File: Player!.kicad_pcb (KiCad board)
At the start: 2 copper layers, 95.2 x 38.1 mm, 25 parts, among them J1 USB4085-GF-A_REVA4, SW1 RotaryEncoder_Switch, SW2 SW_Push, SW3 SW_Push, SW4 SW_Push, SW5 SW_Push, Y1 Crystal

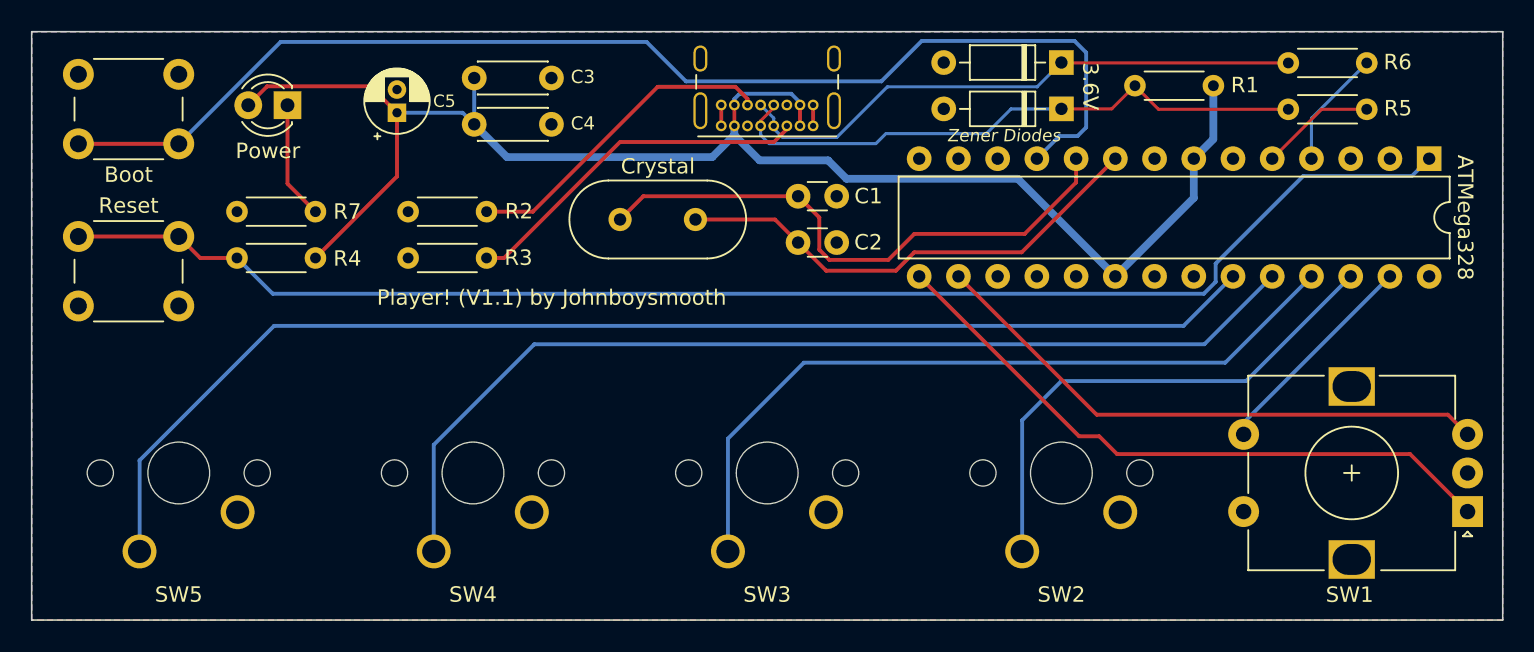
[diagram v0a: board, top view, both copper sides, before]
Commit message: Update PCB
Updated the PCB to include new models for rotary encoder with cap, cherry keys with keycaps. Also reordered some components and added a new horizontal zener diode model
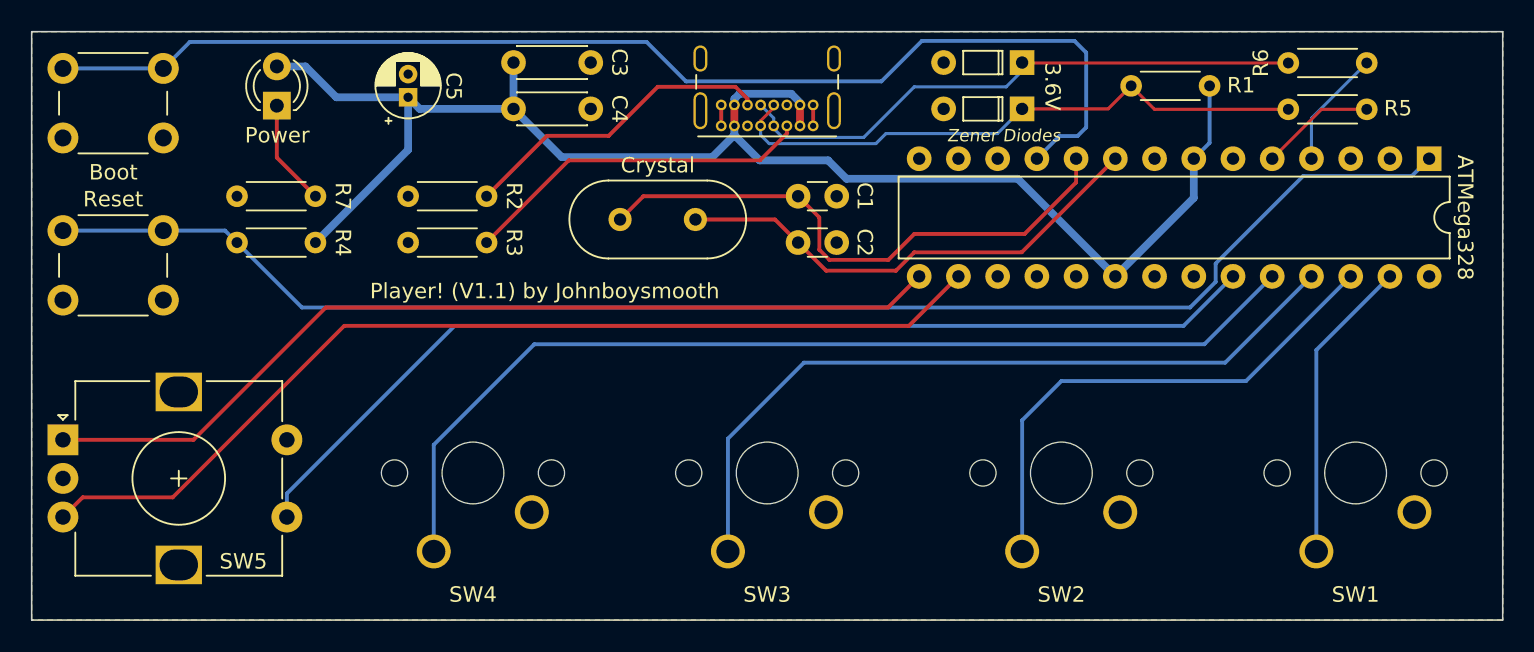
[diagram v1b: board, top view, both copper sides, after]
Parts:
- DN1, DP1: footprint Keyboard Stuff:D_DO-35_SOD27_P7.62mm_Horizontal -> Keyboard Stuff:D_DO-35_SOD27_P5.08mm_Horizontal
- moved SW5 91.1 mm to (2.02, 26.4), turned to 0 degrees
- moved SW1 76.2 mm to (83.2, 33.7)
- moved Boot 8.95 mm to (2.02, 2.38), turned to 0 degrees
- moved R7 5.18 mm to (18.4, 10.7), turned to 180 degrees
- moved C3 2.73 mm to (31.2, 2.00)
- moved C4 2.73 mm to (31.2, 5.00)
- moved DP1 2.55 mm to (64.1, 5.00)
- moved DN1 2.55 mm to (64.1, 2.00)
- moved C5 1.23 mm to (24.4, 4.25)
- moved Reset 1.07 mm to (2.02, 12.9)
- moved R2 1.00 mm to (29.5, 10.7)
- moved R3 1.00 mm to (29.5, 13.7)
- moved R4 1.00 mm to (18.4, 13.7)
- moved Power 0.69 mm to (15.9, 4.79), turned to 90 degrees
- moved R1 0.25 mm to (76.3, 3.51)
- renumbered Y1 to Crystal1, SW5 to SW1, SW1 to SW5
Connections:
- R7 pad 1: GND -> /LED
- R7 pad 2: /LED -> GND
- SW1 pad 1: SW5 -> SW1
- SW5 pad S2: SW1 -> SW5
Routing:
- net ROTB: track 37.2 -> 64.4 mm
- net ROTA: track 41.8 -> 59.8 mm
- net SW5: track 81.6 -> 68.6 mm
- net SW1: track 14.2 -> 19.8 mm
- net /RST: track 93.3 -> 95.2 mm
- net +5V: track 101.1 -> 99.4 mm
- net /BOOT: track 79.3 -> 78.3 mm
- net /LED: track 7.64 -> 6.90 mm
